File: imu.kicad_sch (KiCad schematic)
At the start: 4 parts

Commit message: Added FPGA power component
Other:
- title: (none) -> Inertial measurement unit
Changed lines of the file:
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@@
 (kicad_sch (version 20230121) (generator eeschema)
   (paper "A5")
+  (title_block
+    (title "Inertial measurement unit")
+  )
   (junction (at 128.27 52.07) (diameter 0) (color 0 0 0 0)
   )

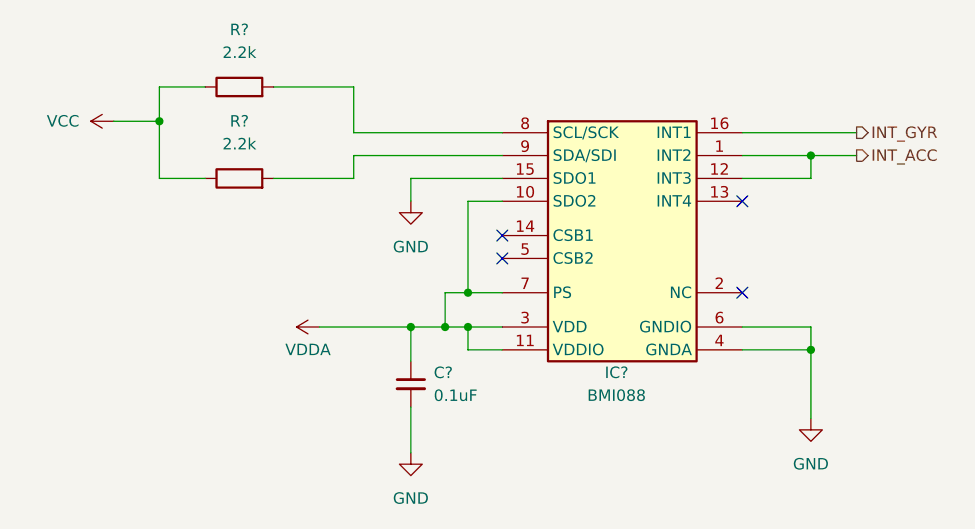
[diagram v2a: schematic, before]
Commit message: Replacing global power labels with hierarchical pins
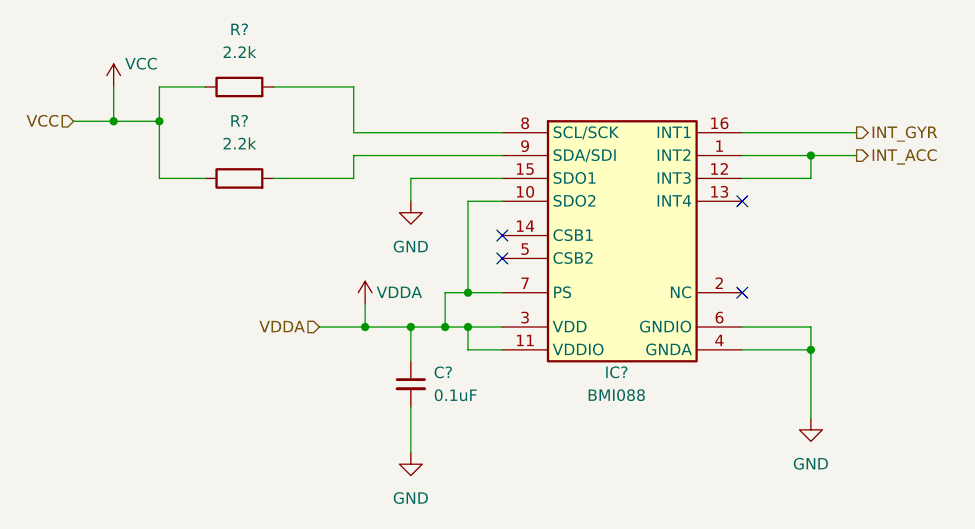
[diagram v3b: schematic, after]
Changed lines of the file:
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@@
   (junction (at 55.88 48.26) (diameter 0) (color 0 0 0 0)
   )
+  (junction (at 78.74 71.12) (diameter 0) (color 0 0 0 0)
+  )
   (junction (at 90.17 71.12) (diameter 0) (color 0 0 0 0)
+  )
+  (junction (at 50.8 48.26) (diameter 0) (color 0 0 0 0)
   )
   (junction (at 87.63 71.12) (diameter 0) (color 0 0 0 0)
@@
     (stroke (width 0) (type default))
   )
-  (wire (pts (xy 73.66 71.12) (xy 83.82 71.12))
+  (wire (pts (xy 46.355 48.26) (xy 50.8 48.26))
+    (stroke (width 0) (type default))
+  )
+  (wire (pts (xy 73.66 71.12) (xy 78.74 71.12))
     (stroke (width 0) (type default))
   )
@@
     (stroke (width 0) (type default))
   )
+  (wire (pts (xy 78.74 68.58) (xy 78.74 71.12))
+    (stroke (width 0) (type default))
+  )
   (wire (pts (xy 120.65 71.12) (xy 128.27 71.12))
     (stroke (width 0) (type default))
@@
     (stroke (width 0) (type default))
   )
+  (wire (pts (xy 50.8 44.45) (xy 50.8 48.26))
+    (stroke (width 0) (type default))
+  )
   (wire (pts (xy 83.82 71.12) (xy 87.63 71.12))
     (stroke (width 0) (type default))
   )
   (wire (pts (xy 120.65 73.66) (xy 128.27 73.66))
+    (stroke (width 0) (type default))
+  )
+  (wire (pts (xy 78.74 71.12) (xy 83.82 71.12))
     (stroke (width 0) (type default))
   )
@@
   (hierarchical_label "INT_GYR" (shape output) (at 133.35 49.53 0) (fields_autoplaced)
     (effects (font (size 1.27 1.27)) (justify left))
+  )
+  (hierarchical_label "VDDA" (shape input) (at 73.66 71.12 180) (fields_autoplaced)
+    (effects (font (size 1.27 1.27)) (justify right))
+  )
+  (hierarchical_label "VCC" (shape input) (at 46.355 48.26 180) (fields_autoplaced)
+    (effects (font (size 1.27 1.27)) (justify right))
   )
   (symbol (lib_id "PCM_4ms_Capacitor:100nF_0603_16V") (at 83.82 77.47 0) (unit 1)
@@
     )
   )
-  (symbol (lib_id "power:VDDA") (at 73.66 71.12 90) (unit 1)
+  (symbol (lib_id "power:VDDA") (at 78.74 68.58 0) (unit 1)
     (in_bom yes) (on_board yes) (dnp no)
-    (property "Reference" "#PWR?" (at 77.47 71.12 0)
-      (effects (font (size 1.27 1.27)) hide)
-    )
-    (property "Value" "VDDA" (at 74.93 73.66 90)
+    (property "Reference" "#PWR?" (at 78.74 72.39 0)
+      (effects (font (size 1.27 1.27)) hide)
+    )
+    (property "Value" "VDDA" (at 80.01 67.31 0)
       (effects (font (size 1.27 1.27)) (justify left))
     )
-    (property "Footprint" "" (at 73.66 71.12 0)
-      (effects (font (size 1.27 1.27)) hide)
-    )
-    (property "Datasheet" "" (at 73.66 71.12 0)
+    (property "Footprint" "" (at 78.74 68.58 0)
+      (effects (font (size 1.27 1.27)) hide)
+    )
+    (property "Datasheet" "" (at 78.74 68.58 0)
       (effects (font (size 1.27 1.27)) hide)
     )
@@
     )
   )
-  (symbol (lib_id "power:VCC") (at 50.8 48.26 90) (unit 1)
-    (in_bom yes) (on_board yes) (dnp no) (fields_autoplaced)
-    (property "Reference" "#PWR?" (at 54.61 48.26 0)
-      (effects (font (size 1.27 1.27)) hide)
-    )
-    (property "Value" "VCC" (at 46.99 48.26 90)
+  (symbol (lib_id "power:VCC") (at 50.8 44.45 0) (unit 1)
+    (in_bom yes) (on_board yes) (dnp no)
+    (property "Reference" "#PWR?" (at 50.8 48.26 0)
+      (effects (font (size 1.27 1.27)) hide)
+    )
+    (property "Value" "VCC" (at 52.07 41.91 0)
       (effects (font (size 1.27 1.27)) (justify left))
     )
-    (property "Footprint" "" (at 50.8 48.26 0)
-      (effects (font (size 1.27 1.27)) hide)
-    )
-    (property "Datasheet" "" (at 50.8 48.26 0)
-      (effects (font (size 1.27 1.27)) hide)
-    )
+    (property "Footprint" "" (at 50.8 44.45 0)
+      (effects (font (size 1.27 1.27)) hide)
+    )
+    (property "Datasheet" "" (at 50.8 44.45 0)
+      (effects (font (size 1.27 1.27)) hide)
+    )

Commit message: Gathering memory components
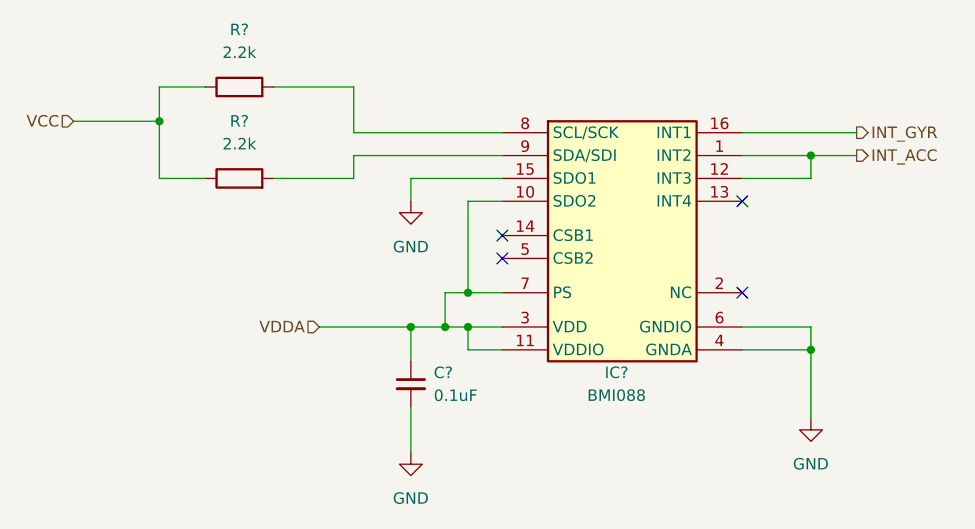
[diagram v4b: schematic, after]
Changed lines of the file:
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@@
   (junction (at 55.88 48.26) (diameter 0) (color 0 0 0 0)
   )
-  (junction (at 78.74 71.12) (diameter 0) (color 0 0 0 0)
-  )
   (junction (at 90.17 71.12) (diameter 0) (color 0 0 0 0)
-  )
-  (junction (at 50.8 48.26) (diameter 0) (color 0 0 0 0)
   )
   (junction (at 87.63 71.12) (diameter 0) (color 0 0 0 0)
@@
     (stroke (width 0) (type default))
   )
-  (wire (pts (xy 50.8 48.26) (xy 55.88 48.26))
-    (stroke (width 0) (type default))
-  )
-  (wire (pts (xy 46.355 48.26) (xy 50.8 48.26))
-    (stroke (width 0) (type default))
-  )
-  (wire (pts (xy 73.66 71.12) (xy 78.74 71.12))
+  (wire (pts (xy 46.355 48.26) (xy 55.88 48.26))
+    (stroke (width 0) (type default))
+  )
+  (wire (pts (xy 73.66 71.12) (xy 83.82 71.12))
     (stroke (width 0) (type default))
   )
@@
     (stroke (width 0) (type default))
   )
-  (wire (pts (xy 78.74 68.58) (xy 78.74 71.12))
-    (stroke (width 0) (type default))
-  )
   (wire (pts (xy 120.65 71.12) (xy 128.27 71.12))
     (stroke (width 0) (type default))
@@
     (stroke (width 0) (type default))
   )
-  (wire (pts (xy 50.8 44.45) (xy 50.8 48.26))
-    (stroke (width 0) (type default))
-  )
   (wire (pts (xy 83.82 71.12) (xy 87.63 71.12))
     (stroke (width 0) (type default))
   )
   (wire (pts (xy 120.65 73.66) (xy 128.27 73.66))
-    (stroke (width 0) (type default))
-  )
-  (wire (pts (xy 78.74 71.12) (xy 83.82 71.12))
     (stroke (width 0) (type default))
   )
@@
         (path "/d34d8324-c983-4098-8d7e-5c2fbd34794d/f15c5f25-9d1e-45fb-9072-66f0c0192516"
           (reference "C1") (unit 1)
-        )
-      )
-    )
-  )
-  (symbol (lib_id "power:VDDA") (at 78.74 68.58 0) (unit 1)
-    (in_bom yes) (on_board yes) (dnp no)
-    (property "Reference" "#PWR?" (at 78.74 72.39 0)
-      (effects (font (size 1.27 1.27)) hide)
-    )
-    (property "Value" "VDDA" (at 80.01 67.31 0)
-      (effects (font (size 1.27 1.27)) (justify left))
-    )
-    (property "Footprint" "" (at 78.74 68.58 0)
-      (effects (font (size 1.27 1.27)) hide)
-    )
-    (property "Datasheet" "" (at 78.74 68.58 0)
-      (effects (font (size 1.27 1.27)) hide)
-    )
-    (pin "1")
-    (instances
-      (project "IMU"
-        (path "/87dd8f57-b26d-490a-9364-62d842a05951"
-          (reference "#PWR?") (unit 1)
-        )
-      )
-      (project "drone"
-        (path "/a9d9e6e7-8403-4088-be51-8a69908fe001/dd672e0a-e58a-4876-8cc0-92f69c93a4a1"
-          (reference "#PWR02") (unit 1)
-        )
-      )
-      (project "drone"
-        (path "/d34d8324-c983-4098-8d7e-5c2fbd34794d/f15c5f25-9d1e-45fb-9072-66f0c0192516"
-          (reference "#PWR03") (unit 1)
         )
       )
@@
         )
       )
-    )
-  )
-  (symbol (lib_id "power:VCC") (at 50.8 44.45 0) (unit 1)
-    (in_bom yes) (on_board yes) (dnp no)
-    (property "Reference" "#PWR?" (at 50.8 48.26 0)
-      (effects (font (size 1.27 1.27)) hide)
-    )
-    (property "Value" "VCC" (at 52.07 41.91 0)
-      (effects (font (size 1.27 1.27)) (justify left))
-    )
-    (property "Footprint" "" (at 50.8 44.45 0)
-      (effects (font (size 1.27 1.27)) hide)
-    )
-    (property "Datasheet" "" (at 50.8 44.45 0)
-      (effects (font (size 1.27 1.27)) hide)
-    )
-    (pin "1")
-    (instances
-      (project "IMU"
-        (path "/87dd8f57-b26d-490a-9364-62d842a05951"
-          (reference "#PWR?") (unit 1)
-        )
-      )
-      (project "drone"
-        (path "/a9d9e6e7-8403-4088-be51-8a69908fe001/dd672e0a-e58a-4876-8cc0-92f69c93a4a1"
-          (reference "#PWR01") (unit 1)
-        )
-      )
-      (project "drone"
-        (path "/d34d8324-c983-4098-8d7e-5c2fbd34794d/f15c5f25-9d1e-45fb-9072-66f0c0192516"
-          (reference "#PWR01") (unit 1)
-        )
-      )
